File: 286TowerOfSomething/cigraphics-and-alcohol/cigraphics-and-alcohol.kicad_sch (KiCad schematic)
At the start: 1 part, among them J1 Bus_ISA_16bit

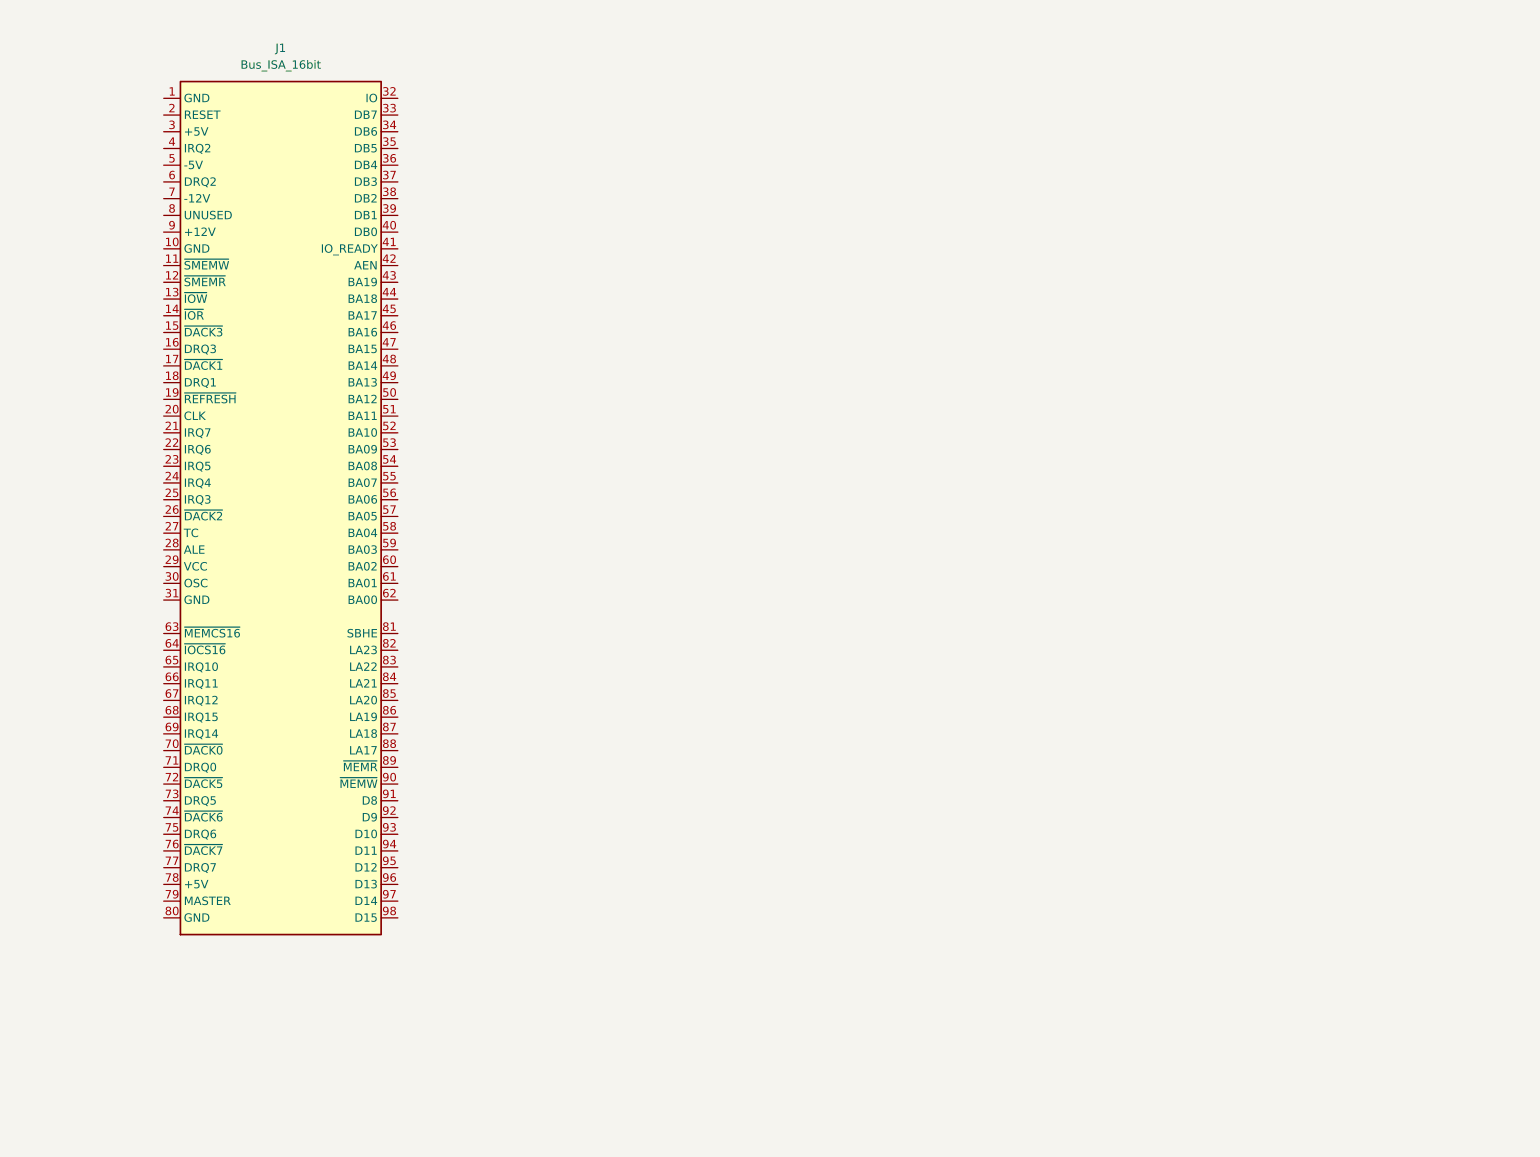
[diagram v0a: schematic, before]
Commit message: Starting on schematic for VGA card
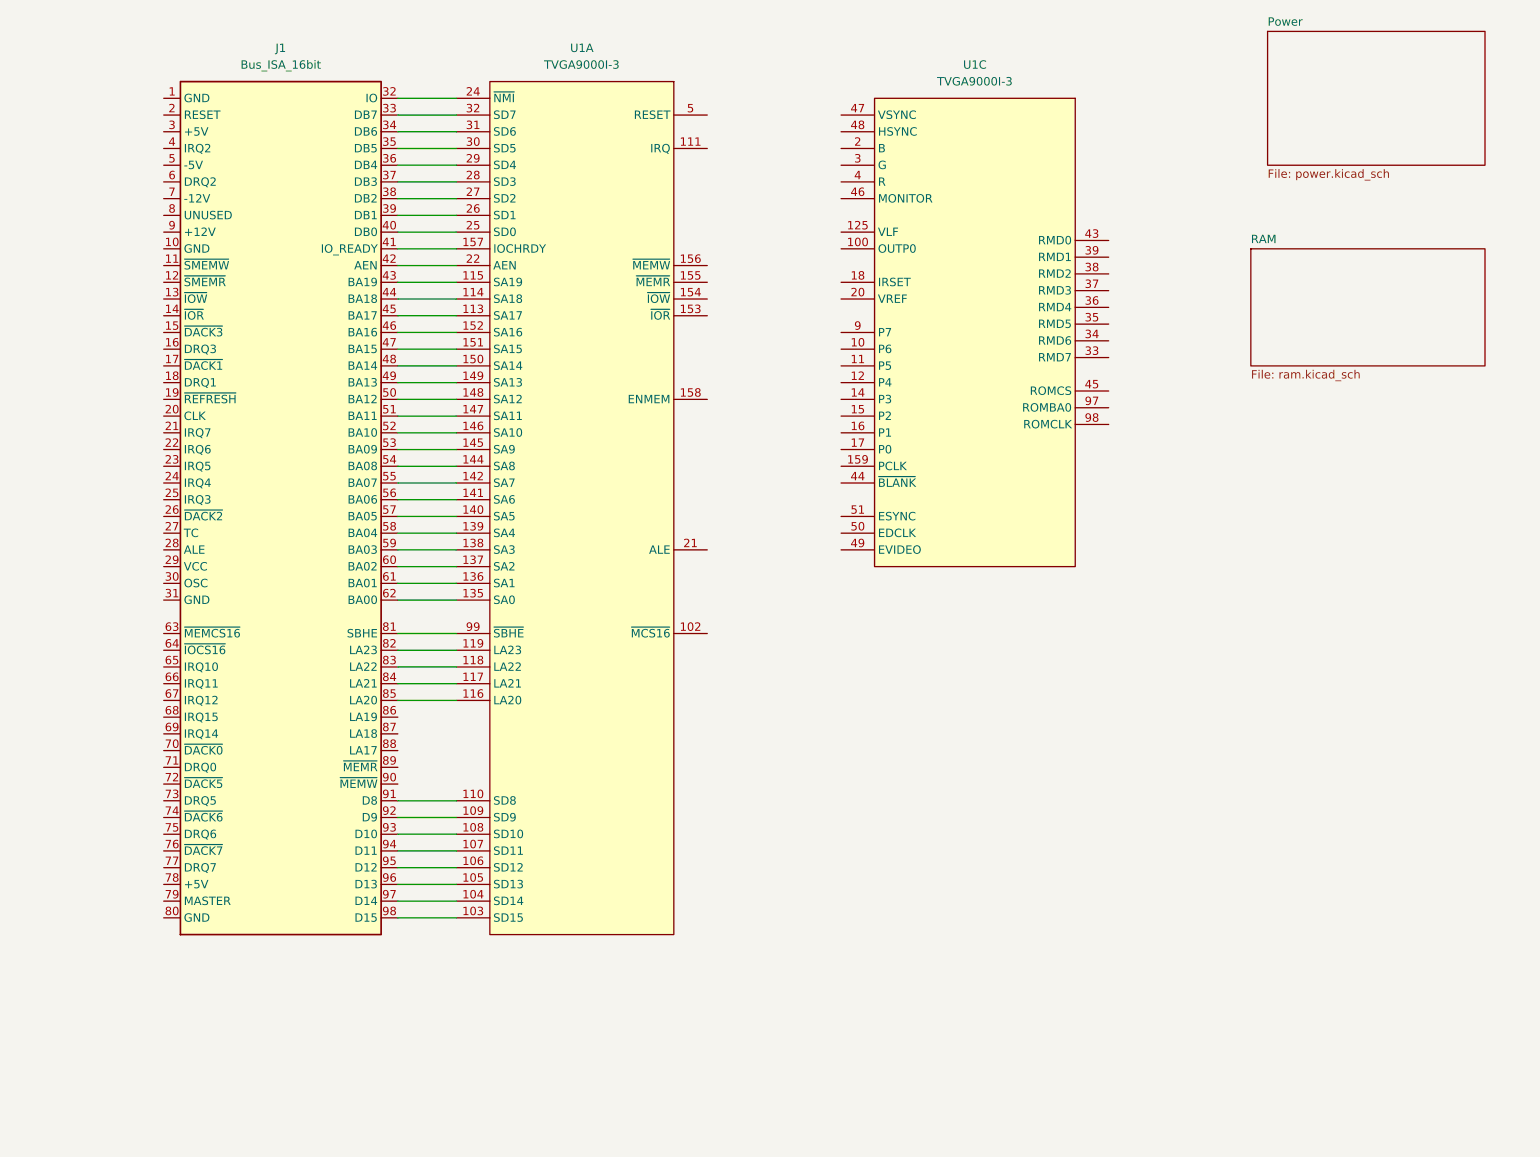
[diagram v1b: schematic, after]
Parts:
- added U1: TVGA9000I-3, Package_QFP:PQFP-160_28x28mm_P0.65mm, symbol pc-parts:TVGA9000i
- J1: footprint (none) -> Connector_PCBEdge:BUS_AT
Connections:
- net at J1.32 (IO): now also U1.24 (~{NMI})
- net at J1.33 (DB7): now also U1.32 (SD7)
- net at J1.34 (DB6): now also U1.31 (SD6)
- net at J1.35 (DB5): now also U1.30 (SD5)
- net at J1.36 (DB4): now also U1.29 (SD4)
- net at J1.37 (DB3): now also U1.28 (SD3)
- net at J1.38 (DB2): now also U1.27 (SD2)
- net at J1.39 (DB1): now also U1.26 (SD1)
- net at J1.40 (DB0): now also U1.25 (SD0)
- net at J1.41 (IO_READY): now also U1.157 (IOCHRDY)
- net at J1.42 (AEN): now also U1.22 (AEN)
- net at J1.43 (BA19): now also U1.115 (SA19)
- net at J1.44 (BA18): now also U1.114 (SA18)
- net at J1.45 (BA17): now also U1.113 (SA17)
- net at J1.46 (BA16): now also U1.152 (SA16)
- net at J1.47 (BA15): now also U1.151 (SA15)
- net at J1.48 (BA14): now also U1.150 (SA14)
- net at J1.49 (BA13): now also U1.149 (SA13)
- net at J1.50 (BA12): now also U1.148 (SA12)
- net at J1.51 (BA11): now also U1.147 (SA11)
- net at J1.52 (BA10): now also U1.146 (SA10)
- net at J1.53 (BA09): now also U1.145 (SA9)
- net at J1.54 (BA08): now also U1.144 (SA8)
- net at J1.55 (BA07): now also U1.142 (SA7)
- net at J1.56 (BA06): now also U1.141 (SA6)
- net at J1.57 (BA05): now also U1.140 (SA5)
- net at J1.58 (BA04): now also U1.139 (SA4)
- net at J1.59 (BA03): now also U1.138 (SA3)
- net at J1.60 (BA02): now also U1.137 (SA2)
- net at J1.61 (BA01): now also U1.136 (SA1)
- net at J1.62 (BA00): now also U1.135 (SA0)
- net at J1.81 (SBHE): now also U1.99 (~{SBHE})
- net at J1.82 (LA23): now also U1.119 (LA23)
- net at J1.83 (LA22): now also U1.118 (LA22)
- net at J1.84 (LA21): now also U1.117 (LA21)
- net at J1.85 (LA20): now also U1.116 (LA20)
- net at J1.91 (D8): now also U1.110 (SD8)
- net at J1.92 (D9): now also U1.109 (SD9)
- net at J1.93 (D10): now also U1.108 (SD10)
- net at J1.94 (D11): now also U1.107 (SD11)
- net at J1.95 (D12): now also U1.106 (SD12)
- net at J1.96 (D13): now also U1.105 (SD13)
- net at J1.97 (D14): now also U1.104 (SD14)
- net at J1.98 (D15): now also U1.103 (SD15)
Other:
- added sheet Power (power.kicad_sch)
- added sheet RAM (ram.kicad_sch)

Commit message: Almost finished schematic for cigraphics-and-alcohol
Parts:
- removed unit 3 of U1
- added C28: 470p, Capacitor_SMD:C_0603_1608Metric_Pad1.08x0.95mm_HandSolder, symbol Device:C
- added C29: 47p, Capacitor_SMD:C_0603_1608Metric_Pad1.08x0.95mm_HandSolder, symbol Device:C
- added C30: 100p, Capacitor_SMD:C_0603_1608Metric_Pad1.08x0.95mm_HandSolder, symbol Device:C
- added R6: 1K, Resistor_SMD:R_0603_1608Metric_Pad0.98x0.95mm_HandSolder, symbol Device:R
- added R7: 100, Resistor_SMD:R_0603_1608Metric_Pad0.98x0.95mm_HandSolder, symbol Device:R
- added SW1: SW_DIP_x05, symbol Switch:SW_DIP_x05
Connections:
- net GND: now reaches J1.1 (GND)
- net GND: now also J1.10 (GND), J1.31 (GND), J1.80 (GND), C28.2, C29.2, C30.2, SW1.2, SW1.3, SW1.4, SW1.5
- net ~{MEMW}: now reaches J1.11 (~{SMEMW})
- net ~{MEMW}: now also U1.156 (~{MEMW})
- net ~{MEMR}: now reaches J1.12 (~{SMEMR})
- net ~{MEMR}: now also U1.155 (~{MEMR}), C29.1
- net ~{IOW}: now reaches J1.13 (~{IOW})
- net ~{IOW}: now also R7.2
- net ~{IOR}: now reaches J1.14 (~{IOR})
- net ~{IOR}: now also U1.153 (~{IOR})
- net ~{REFRESH}: now reaches J1.19 (~{REFRESH})
- net ~{REFRESH}: now also U1.158 (ENMEM)
- net RESET: now reaches J1.2 (RESET)
- net RESET: now also R6.2
- net ALE: now reaches J1.28 (ALE)
- net ALE: now also U1.21 (ALE)
- net +5V: now reaches J1.29 (VCC)
- net +5V: now also J1.3 (+5V), J1.78 (+5V)
- net OSC: now reaches J1.30 (OSC)
- net IRQ: now reaches J1.4 (IRQ2)
- net IRQ: now also SW1.1
- net A14: now reaches J1.48 (BA14), U1.150 (SA14)
- net A13: now reaches J1.49 (BA13), U1.149 (SA13)
- net A12: now reaches J1.50 (BA12), U1.148 (SA12)
- net A11: now reaches J1.51 (BA11), U1.147 (SA11)
- net A10: now reaches J1.52 (BA10), U1.146 (SA10)
- net A9: now reaches J1.53 (BA09), U1.145 (SA9)
- net A8: now reaches J1.54 (BA08), U1.144 (SA8)
- net A7: now reaches J1.55 (BA07), U1.142 (SA7)
- net A6: now reaches J1.56 (BA06), U1.141 (SA6)
- net A5: now reaches J1.57 (BA05), U1.140 (SA5)
- net A4: now reaches J1.58 (BA04), U1.139 (SA4)
- net A3: now reaches J1.59 (BA03), U1.138 (SA3)
- net A2: now reaches J1.60 (BA02), U1.137 (SA2)
- net A1: now reaches J1.61 (BA01), U1.136 (SA1)
- net ~{MEMCS16}: now reaches J1.63 (~{MEMCS16})
- net ~{MEMCS16}: now also U1.102 (~{MCS16})
- net IRQ_SW: now reaches U1.111 (IRQ)
- net IRQ_SW: now also SW1.10
- net at U1.154 (~{IOW}): now also C30.1, R7.1
- net at U1.5 (RESET): now also C28.1, R6.1
- new net Analog/RMD5: SW1.6
- new net Analog/RMD7: SW1.7
- new net RAM/MD2: SW1.8
- new net RAM/MD7: SW1.9
- no-connect marks 0 -> 32
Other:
- added sheet Analog (analog.kicad_sch)
- sheet RAM ports: added MD2, MD7; removed none

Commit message: I swear bro, just one more cap...
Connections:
- no-connect marks 32 -> 37
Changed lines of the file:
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@@
+	)
+	(no_connect
+		(at 83.82 132.08)
 	)
 	(no_connect
@@
 	)
 	(no_connect
+		(at 83.82 134.62)
+	)
+	(no_connect
 		(at 48.26 76.2)
 	)
@@
 	(no_connect
 		(at 48.26 50.8)
+	)
+	(no_connect
+		(at 83.82 127)
 	)
 	(no_connect
@@
 	)
 	(no_connect
+		(at 83.82 129.54)
+	)
+	(no_connect
 		(at 48.26 99.06)
 	)
@@
 	)
 	(no_connect
+		(at 83.82 137.16)
+	)
+	(no_connect

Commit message: Adding bracket to graphics card
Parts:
- added U7: ~, pc-parts:PC_BRACKET_ISA_KEYSTONE_9200_Rev1_1, symbol pc-parts:9202
- SW1: footprint (none) -> Button_Switch_THT:SW_DIP_SPSTx05_Slide_9.78x14.88mm_W7.62mm_P2.54mm
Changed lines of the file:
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@@
 			)
 		)
-		(property "Footprint" ""
+		(property "Footprint" "Button_Switch_THT:SW_DIP_SPSTx05_Slide_9.78x14.88mm_W7.62mm_P2.54mm"
 			(at 177.8 135.89 0)
 			(effects
@@
 					(unit 1)
 				)
+			)
+		)
+	)
+	(symbol
+		(lib_id "pc-parts:9202")
+		(at 152.4 190.5 0)
+		(unit 1)
+		(exclude_from_sim no)
+		(in_bom yes)
+		(on_board yes)
+		(dnp no)
+		(fields_autoplaced yes)
+		(property "Reference" "U7"
+			(at 152.4 190.5 0)
+			(effects
+				(font
+					(size 1.27 1.27)
+				)
+				(hide yes)
+			)
+		)
+		(property "Value" "~"
+			(at 157.48 190.5 0)
+			(effects
+				(font
+					(size 1.27 1.27)
+				)
+				(justify left)
+			)
+		)
+		(property "Footprint" "pc-parts:PC_BRACKET_ISA_KEYSTONE_9200_Rev1_1"
+			(at 152.4 190.5 0)
+			(effects
+				(font
+					(size 1.27 1.27)
+				)
+				(hide yes)
+			)
+		)
+		(property "Datasheet" ""
+			(at 152.4 190.5 0)
+			(effects
+				(font
+					(size 1.27 1.27)
+				)
+				(hide yes)
+			)
+		)
+		(property "Description" ""
+			(at 152.4 190.5 0)
+			(effects
+				(font
+					(size 1.27 1.27)
+				)
+				(hide yes)
+			)
+		)
+		(instances
+			(project ""
+				(path "/e0e6ae0e-7043-40c9-b78f-5dfbc2956e88"
+					(reference "U7")
+					(unit 1)
+				)
